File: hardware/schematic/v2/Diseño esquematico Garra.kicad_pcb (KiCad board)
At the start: 2 copper layers, 85.5 x 137 mm, 18 parts

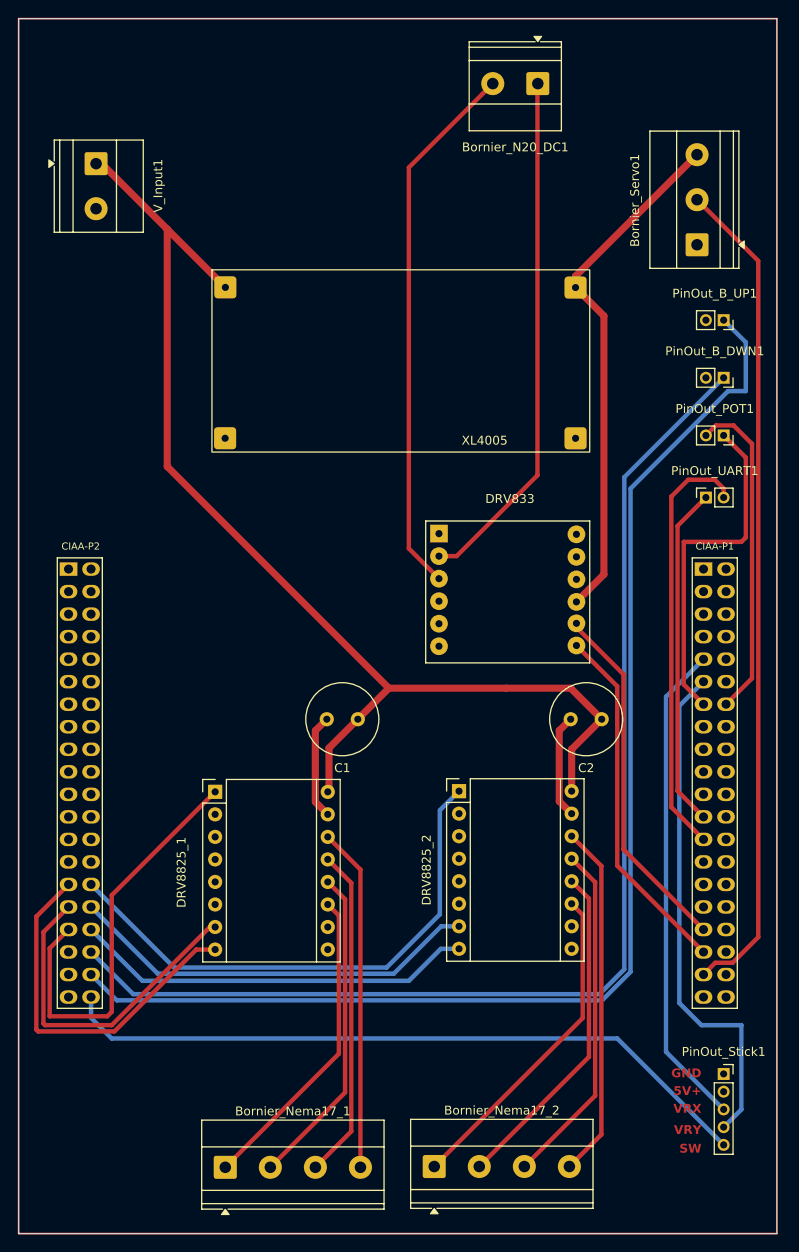
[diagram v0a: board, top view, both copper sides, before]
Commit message: fix: PCB border colision
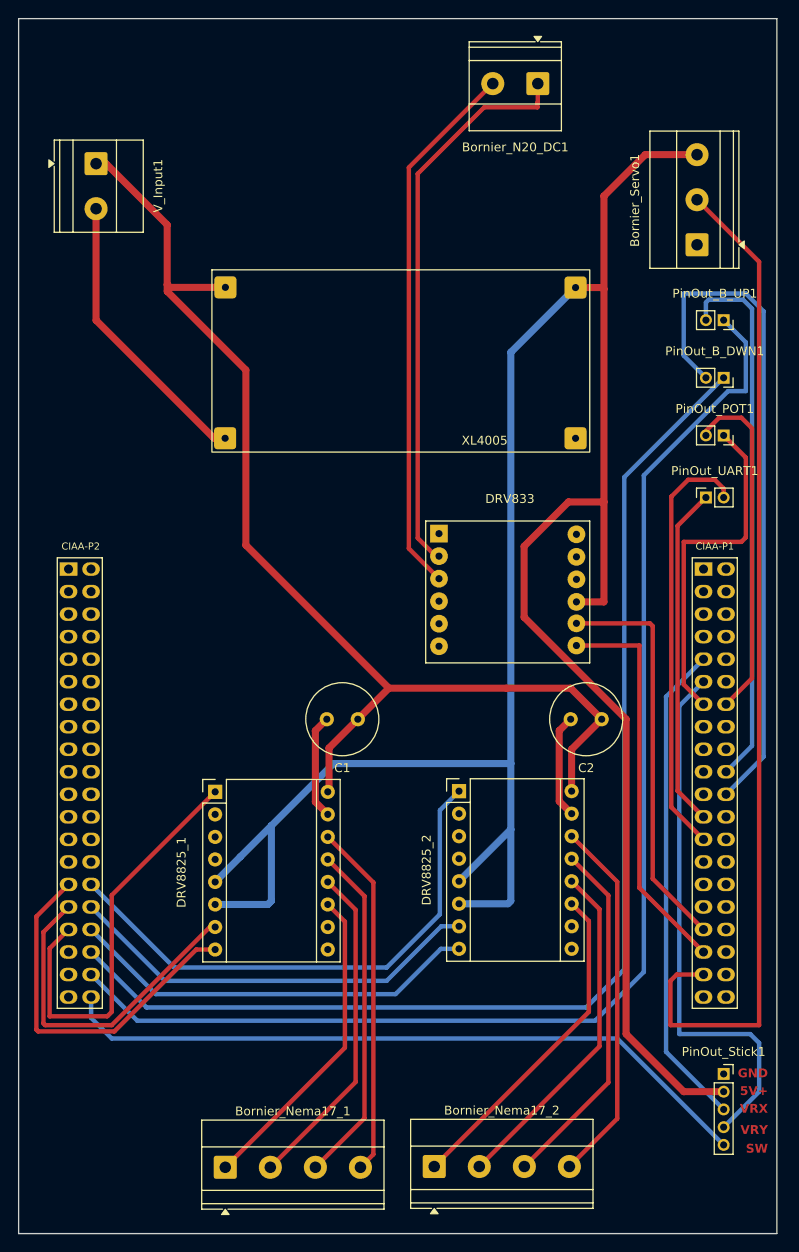
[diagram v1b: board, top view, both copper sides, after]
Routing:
- net 5V: track 58.7 -> 289.4 mm
- net GND_B_DWN: track 0.00 -> 76.6 mm
- net GND_B_UP: track 0.00 -> 61.2 mm
- net GND: track 23.6 -> 56.3 mm
- net SERVO_PWM: track 93.9 -> 115.0 mm
- net IN2: track 40.5 -> 45.3 mm
- net MOTOR_VCC: track 59.4 -> 63.7 mm
- net IN1: track 40.9 -> 45.0 mm
- net VRY: track 57.7 -> 61.4 mm
- net B_UP: track 144.4 -> 147.2 mm
- net GND_POT: track 37.1 -> 39.1 mm
- net B2_2: track 40.1 -> 41.6 mm
- net B_DWN: track 134.6 -> 135.8 mm
- net DIR2: track 45.4 -> 46.6 mm
- net B1_2: track 39.1 -> 40.3 mm
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
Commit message: feat: Copper layers added to the PCB
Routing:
- net GND_Stick: track 0.00 -> 55.7 mm
- net GND: track 56.3 -> 23.6 mm
- net VRX: track 55.2 -> 59.1 mm
- added copper zone on B.Cu, net GND
- added copper zone on F.Cu, net GND
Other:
- board text removed: "5V+"
- board text removed: "GND"
- board text removed: "SW"
- board text removed: "VRX"
- board text removed: "VRY"
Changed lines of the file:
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@@
 		(layer "Edge.Cuts")
-	)
-	(gr_text "VRY\n\n"
-		(at 119.5 152.5 0)
-		(layer "F.Cu")
-		(effects
-			(font
-				(size 1 1)
-				(thickness 0.2)
-				(bold yes)
-			)
-			(justify right bottom)
-		)
-	)
-	(gr_text "GND"
-		(at 119.5 144.5 0)
-		(layer "F.Cu")
-		(effects
-			(font
-				(size 1 1)
-				(thickness 0.2)
-				(bold yes)
-			)
-			(justify right bottom)
-		)
-	)
-	(gr_text "5V+\n"
-		(at 119.5 146.5 0)
-		(layer "F.Cu")
-		(effects
-			(font
-				(size 1 1)
-				(thickness 0.2)
-				(bold yes)
-			)
-			(justify right bottom)
-		)
-	)
-	(gr_text "SW"
-		(at 119.5 153 0)
-		(layer "F.Cu")
-		(effects
-			(font
-				(size 1 1)
-				(thickness 0.2)
-				(bold yes)
-			)
-			(justify right bottom)
-		)
-	)
-	(gr_text "VRX\n"
-		(at 119.5 148.5 0)
-		(layer "F.Cu")
-		(effects
-			(font
-				(size 1 1)
-				(thickness 0.2)
-				(bold yes)
-			)
-			(justify right bottom)
-		)
 	)
 	(segment
@@
 	)
 	(segment
-		(start 58.283641 72.317886)
-		(end 57.033641 72.317886)
-		(width 0.8)
-		(layer "F.Cu")
-		(net 13)
-	)
-	(segment
-		(start 57.033641 72.317886)
-		(end 43.734016 59.018261)
-		(width 0.8)
-		(layer "F.Cu")
-		(net 13)
-	)
-	(segment
 		(start 97.36 114.65)
 		(end 95.959 113.249)
@@
 	)
 	(segment
-		(start 43.734016 59.018261)
-		(end 43.734016 46.433675)
-		(width 0.8)
-		(layer "F.Cu")
-		(net 13)
-	)
-	(segment
 		(start 95.959 105.291)
 		(end 97.25 104)
@@
 	)
 	(segment
-		(start 108 101.46)
+		(start 107 140.5)
+		(end 107 97.23)
+		(width 0.5)
+		(layer "B.Cu")
+		(net 17)
+	)
+	(segment
+		(start 114.5 148)
+		(end 107 140.5)
+		(width 0.5)
+		(layer "B.Cu")
+		(net 17)
+	)
+	(segment
+		(start 107 97.23)
 		(end 112.23 97.23)
-		(width 0.5)
-		(layer "B.Cu")
-		(net 17)
-	)
-	(segment
-		(start 114.5 148)
-		(end 108 141.5)
-		(width 0.5)
-		(layer "B.Cu")
-		(net 17)
-	)
-	(segment
-		(start 108 141.5)
-		(end 108 101.46)
 		(width 0.5)
 		(layer "B.Cu")
@@
 	)
 	(segment
+		(start 113.008636 144)
+		(end 108.5 139.491364)
+		(width 0.5)
+		(layer "B.Cu")
+		(net 21)
+	)
+	(segment
+		(start 113.5 98.5)
+		(end 114.77 99.77)
+		(width 0.5)
+		(layer "B.Cu")
+		(net 21)
+	)
+	(segment
+		(start 114.5 144)
+		(end 113.008636 144)
+		(width 0.5)
+		(layer "B.Cu")
+		(net 21)
+	)
+	(segment
+		(start 108.5 98.5)
+		(end 113.5 98.5)
+		(width 0.5)
+		(layer "B.Cu")
+		(net 21)
+	)
+	(segment
+		(start 108.5 139.491364)
+		(end 108.5 98.5)
+		(width 0.5)
+		(layer "B.Cu")
+		(net 21)
+	)
+	(segment
 		(start 38 138.5)
 		(end 45.5 138.5)
@@
 		(net 86)
 	)
+	(zone
+		(net 13)
+		(net_name "GND")
+		(layers "F.Cu" "B.Cu")
+		(hatch edge 0.5)
+		(connect_pads yes
+			(clearance 0.5)
+		)
+		(min_thickness 0.25)
+		(filled_areas_thickness no)
+		(fill yes
+			(thermal_gap 0.5)
+			(thermal_bridge_width 0.5)
+		)
+		(polygon
+			(pts
+				(xy 35.5 25.5) (xy 35.5 161.5) (xy 120 161.5) (xy 120 25.5)
+			)
+		)
+	)
 	(embedded_fonts no)
